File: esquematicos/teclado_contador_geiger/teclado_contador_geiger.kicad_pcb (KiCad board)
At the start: 2 copper layers, 14 parts, among them J1 Conn_01x04_Female, SW1 SW_SPST, SW2 SW_SPST, SW3 SW_SPST, SW4 SW_SPST, SW5 SW_SPST, SW6 SW_SPST

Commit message: Agregado del PCB del teclado(2)
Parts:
- J1: footprint Connector_JST:JST_EH_B04B-EH-A_1x04_P2.50mm_Vertical -> Connector_JST:JST_XH_B04B-XH-A_1x04_P2.50mm_Vertical
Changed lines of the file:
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@@
   )
   (setup
-    (last_trace_width 1.27)
+    (last_trace_width 0.25)
     (user_trace_width 1.27)
     (trace_clearance 0.2)
@@
     )
   )
-  (module Connector_JST:JST_EH_B04B-EH-A_1x04_P2.50mm_Vertical (layer B.Cu)
-    (at 130.81 102.616)
-    (descr "JST EH series connector, B04B-EH-A (http://www.jst-mfg.com/product/pdf/eng/eEH.pdf), generated with kicad-footprint-generator")
-    (tags "connector JST EH side entry")
-    (fp_text reference J1 (at 3.75 2.8) (layer B.SilkS)
-      (effects (font (size 1 1) (thickness 0.15)) (justify mirror))
-    )
-    (fp_text value Conn_01x04_Female (at 3.75 -3.4) (layer B.Fab)
-      (effects (font (size 1 1) (thickness 0.15)) (justify mirror))
-    )
-    (fp_line (start -2.5 1.6) (end -2.5 -2.2) (layer B.Fab) (width 0.1))
-    (fp_line (start -2.5 -2.2) (end 10 -2.2) (layer B.Fab) (width 0.1))
-    (fp_line (start 10 -2.2) (end 10 1.6) (layer B.Fab) (width 0.1))
-    (fp_line (start 10 1.6) (end -2.5 1.6) (layer B.Fab) (width 0.1))
-    (fp_line (start -3 2.1) (end -3 -2.7) (layer B.CrtYd) (width 0.05))
-    (fp_line (start -3 -2.7) (end 10.5 -2.7) (layer B.CrtYd) (width 0.05))
-    (fp_line (start 10.5 -2.7) (end 10.5 2.1) (layer B.CrtYd) (width 0.05))
-    (fp_line (start 10.5 2.1) (end -3 2.1) (layer B.CrtYd) (width 0.05))
-    (fp_line (start -2.61 1.71) (end -2.61 -2.31) (layer B.SilkS) (width 0.12))
-    (fp_line (start -2.61 -2.31) (end 10.11 -2.31) (layer B.SilkS) (width 0.12))
-    (fp_line (start 10.11 -2.31) (end 10.11 1.71) (layer B.SilkS) (width 0.12))
-    (fp_line (start 10.11 1.71) (end -2.61 1.71) (layer B.SilkS) (width 0.12))
-    (fp_line (start -2.61 0) (end -2.11 0) (layer B.SilkS) (width 0.12))
-    (fp_line (start -2.11 0) (end -2.11 1.21) (layer B.SilkS) (width 0.12))
-    (fp_line (start -2.11 1.21) (end 9.61 1.21) (layer B.SilkS) (width 0.12))
-    (fp_line (start 9.61 1.21) (end 9.61 0) (layer B.SilkS) (width 0.12))
-    (fp_line (start 9.61 0) (end 10.11 0) (layer B.SilkS) (width 0.12))
-    (fp_line (start -2.61 -0.81) (end -1.61 -0.81) (layer B.SilkS) (width 0.12))
-    (fp_line (start -1.61 -0.81) (end -1.61 -2.31) (layer B.SilkS) (width 0.12))
-    (fp_line (start 10.11 -0.81) (end 9.11 -0.81) (layer B.SilkS) (width 0.12))
-    (fp_line (start 9.11 -0.81) (end 9.11 -2.31) (layer B.SilkS) (width 0.12))
-    (fp_line (start -2.91 -0.11) (end -2.91 -2.61) (layer B.SilkS) (width 0.12))
-    (fp_line (start -2.91 -2.61) (end -0.41 -2.61) (layer B.SilkS) (width 0.12))
-    (fp_line (start -2.91 -0.11) (end -2.91 -2.61) (layer B.Fab) (width 0.1))
-    (fp_line (start -2.91 -2.61) (end -0.41 -2.61) (layer B.Fab) (width 0.1))
-    (fp_text user %R (at 3.75 -1.5) (layer B.Fab)
-      (effects (font (size 1 1) (thickness 0.15)) (justify mirror))
-    )
-    (pad 1 thru_hole roundrect (at 0 0) (size 1.7 1.95) (drill 0.95) (layers *.Cu *.Mask) (roundrect_rratio 0.147059)
-      (net 3 +5V))
-    (pad 2 thru_hole oval (at 2.5 0) (size 1.7 1.95) (drill 0.95) (layers *.Cu *.Mask)
-      (net 4 GND))
-    (pad 3 thru_hole oval (at 5 0) (size 1.7 1.95) (drill 0.95) (layers *.Cu *.Mask)
-      (net 5 /teclado_out))
-    (pad 4 thru_hole oval (at 7.5 0) (size 1.7 1.95) (drill 0.95) (layers *.Cu *.Mask)
-      (net 1 "Net-(D1-Pad1)"))
-    (model ${KISYS3DMOD}/Connector_JST.3dshapes/JST_EH_B04B-EH-A_1x04_P2.50mm_Vertical.wrl
-      (at (xyz 0 0 0))
-      (scale (xyz 1 1 1))
-      (rotate (xyz 0 0 0))
-    )
-  )
   (module Resistor_SMD:R_0805_2012Metric_Pad1.15x1.40mm_HandSolder (layer B.Cu)
     (at 147.066 85.852 180)
@@
       (at (xyz 0 0 0))
       (scale (xyz 1 1 1))
+      (rotate (xyz 0 0 0))
+    )
+  )
+  (module Connector_JST:JST_XH_B04B-XH-A_1x04_P2.50mm_Vertical (layer B.Cu)
+    (at 130.81 102.616)
+    (descr "JST XH series connector, B04B-XH-A (http://www.jst-mfg.com/product/pdf/eng/eXH.pdf), generated with kicad-footprint-generator")
+    (tags "connector JST XH side entry")
+    (fp_text reference J1 (at 3.75 3.55) (layer B.SilkS)
+      (effects (font (size 1 1) (thickness 0.15)) (justify mirror))
+    )
+    (fp_text value Conn_01x04_Female (at 3.75 -4.6) (layer B.Fab)
+      (effects (font (size 1 1) (thickness 0.15)) (justify mirror))
+    )
+    (fp_line (start -2.45 2.35) (end -2.45 -3.4) (layer B.Fab) (width 0.1))
+    (fp_line (start -2.45 -3.4) (end 9.95 -3.4) (layer B.Fab) (width 0.1))
+    (fp_line (start 9.95 -3.4) (end 9.95 2.35) (layer B.Fab) (width 0.1))
+    (fp_line (start 9.95 2.35) (end -2.45 2.35) (layer B.Fab) (width 0.1))
+    (fp_line (start -2.56 2.46) (end -2.56 -3.51) (layer B.SilkS) (width 0.12))
+    (fp_line (start -2.56 -3.51) (end 10.06 -3.51) (layer B.SilkS) (width 0.12))
+    (fp_line (start 10.06 -3.51) (end 10.06 2.46) (layer B.SilkS) (width 0.12))
+    (fp_line (start 10.06 2.46) (end -2.56 2.46) (layer B.SilkS) (width 0.12))
+    (fp_line (start -2.95 2.85) (end -2.95 -3.9) (layer B.CrtYd) (width 0.05))
+    (fp_line (start -2.95 -3.9) (end 10.45 -3.9) (layer B.CrtYd) (width 0.05))
+    (fp_line (start 10.45 -3.9) (end 10.45 2.85) (layer B.CrtYd) (width 0.05))
+    (fp_line (start 10.45 2.85) (end -2.95 2.85) (layer B.CrtYd) (width 0.05))
+    (fp_line (start -0.625 2.35) (end 0 1.35) (layer B.Fab) (width 0.1))
+    (fp_line (start 0 1.35) (end 0.625 2.35) (layer B.Fab) (width 0.1))
+    (fp_line (start 0.75 2.45) (end 0.75 1.7) (layer B.SilkS) (width 0.12))
+    (fp_line (start 0.75 1.7) (end 6.75 1.7) (layer B.SilkS) (width 0.12))
+    (fp_line (start 6.75 1.7) (end 6.75 2.45) (layer B.SilkS) (width 0.12))
+    (fp_line (start 6.75 2.45) (end 0.75 2.45) (layer B.SilkS) (width 0.12))
+    (fp_line (start -2.55 2.45) (end -2.55 1.7) (layer B.SilkS) (width 0.12))
+    (fp_line (start -2.55 1.7) (end -0.75 1.7) (layer B.SilkS) (width 0.12))
+    (fp_line (start -0.75 1.7) (end -0.75 2.45) (layer B.SilkS) (width 0.12))
+    (fp_line (start -0.75 2.45) (end -2.55 2.45) (layer B.SilkS) (width 0.12))
+    (fp_line (start 8.25 2.45) (end 8.25 1.7) (layer B.SilkS) (width 0.12))
+    (fp_line (start 8.25 1.7) (end 10.05 1.7) (layer B.SilkS) (width 0.12))
+    (fp_line (start 10.05 1.7) (end 10.05 2.45) (layer B.SilkS) (width 0.12))
+    (fp_line (start 10.05 2.45) (end 8.25 2.45) (layer B.SilkS) (width 0.12))
+    (fp_line (start -2.55 0.2) (end -1.8 0.2) (layer B.SilkS) (width 0.12))
+    (fp_line (start -1.8 0.2) (end -1.8 -2.75) (layer B.SilkS) (width 0.12))
+    (fp_line (start -1.8 -2.75) (end 3.75 -2.75) (layer B.SilkS) (width 0.12))
+    (fp_line (start 10.05 0.2) (end 9.3 0.2) (layer B.SilkS) (width 0.12))
+    (fp_line (start 9.3 0.2) (end 9.3 -2.75) (layer B.SilkS) (width 0.12))
+    (fp_line (start 9.3 -2.75) (end 3.75 -2.75) (layer B.SilkS) (width 0.12))
+    (fp_line (start -1.6 2.75) (end -2.85 2.75) (layer B.SilkS) (width 0.12))
+    (fp_line (start -2.85 2.75) (end -2.85 1.5) (layer B.SilkS) (width 0.12))
+    (fp_text user %R (at 3.75 -2.7) (layer B.Fab)
+      (effects (font (size 1 1) (thickness 0.15)) (justify mirror))
+    )
+    (pad 1 thru_hole roundrect (at 0 0) (size 1.7 1.95) (drill 0.95) (layers *.Cu *.Mask) (roundrect_rratio 0.147059)
+      (net 3 +5V))
+    (pad 2 thru_hole oval (at 2.5 0) (size 1.7 1.95) (drill 0.95) (layers *.Cu *.Mask)
+      (net 4 GND))
+    (pad 3 thru_hole oval (at 5 0) (size 1.7 1.95) (drill 0.95) (layers *.Cu *.Mask)
+      (net 5 /teclado_out))
+    (pad 4 thru_hole oval (at 7.5 0) (size 1.7 1.95) (drill 0.95) (layers *.Cu *.Mask)
+      (net 1 "Net-(D1-Pad1)"))
+    (model ${KISYS3DMOD}/Connector_JST.3dshapes/JST_XH_B04B-XH-A_1x04_P2.50mm_Vertical.wrl
+      (at (xyz 0 0 0))
+      (scale (xyz 1 1 1))

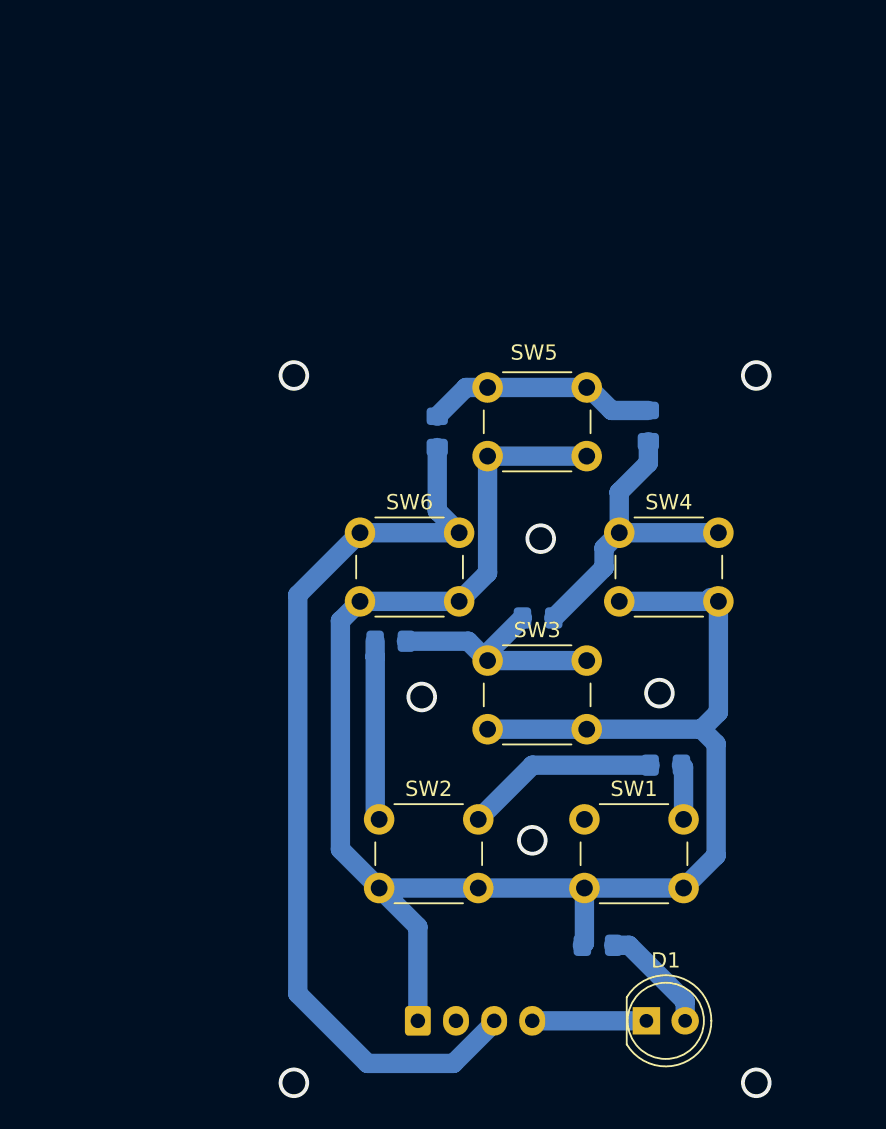
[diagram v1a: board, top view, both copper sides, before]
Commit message: Agregado de LED verde a la placa del teclado e incremento de las dimensiones de esta última incluyendo una mayor separación entre los botones
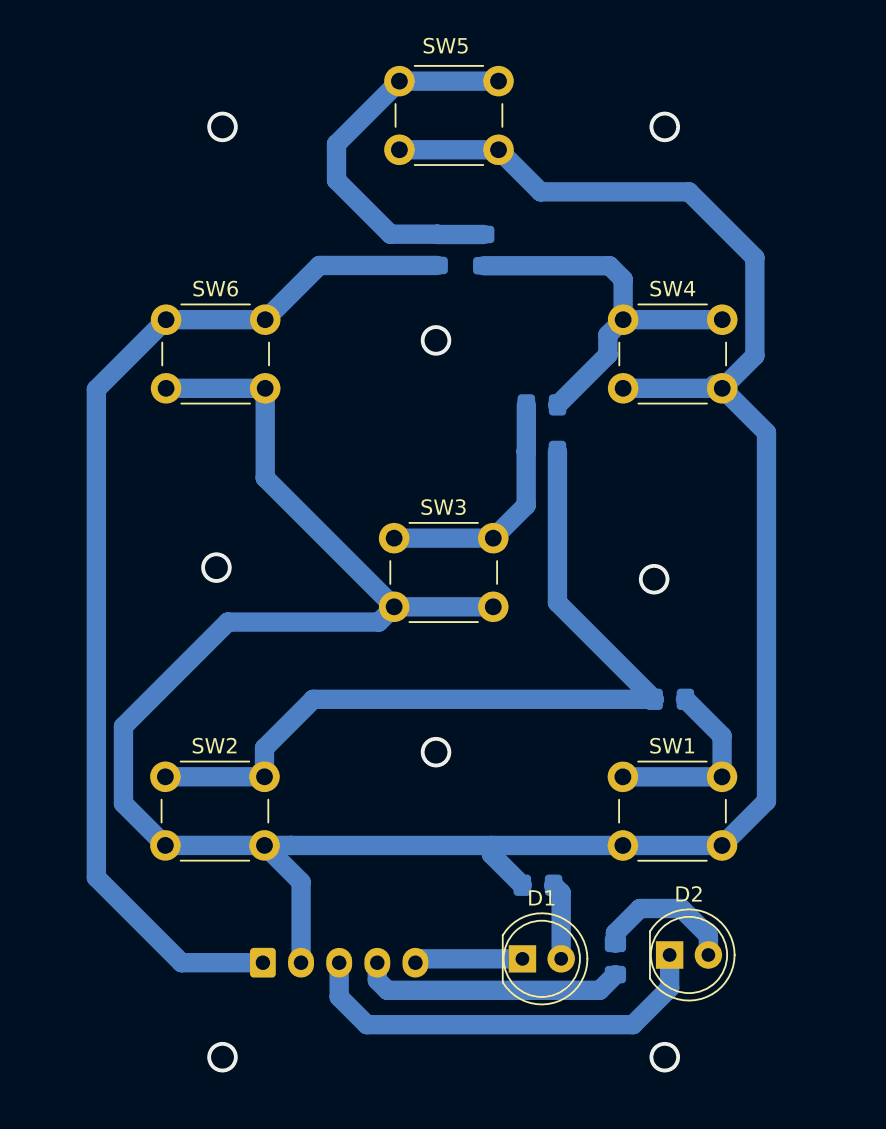
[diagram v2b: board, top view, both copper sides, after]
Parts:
- added D2: LED VERDE, LED_THT:LED_D5.0mm, F.Cu at (147.3, 98.3)
- added R7: 220, Resistor_SMD:R_0805_2012Metric_Pad1.15x1.40mm_HandSolder, B.Cu at (143.8, 98.6)
- D1: value LED -> LED ROJO
- J1: value Conn_01x04_Female -> Conn_01x05_Female; footprint Connector_JST:JST_XH_B04B-XH-A_1x04_P2.50mm_Vertical -> Connector_JST:JST_XH_B05B-XH-A_1x05_P2.50mm_Vertical
- moved SW5 20.9 mm to (129.6, 41.0)
- moved SW6 18.9 mm to (114.3, 56.6)
- moved R2 15.9 mm to (138.9, 65.3), turned to 180 degrees
- moved R4 15.8 mm to (135.1, 52.1)
- moved SW2 14.3 mm to (114.3, 86.6)
- moved R3 14.0 mm to (138.9, 62.2)
- moved SW4 14.0 mm to (144.3, 56.6)
- moved R5 11.9 mm to (132.1, 52.1)
- moved J1 10.9 mm to (120.7, 98.8)
- moved SW3 10.1 mm to (129.3, 71.0)
- moved D1 9.09 mm to (137.7, 98.6)
- moved R6 5.57 mm to (138.7, 93.7)
- moved R1 4.33 mm to (147.3, 81.5)
- moved SW1 3.76 mm to (144.3, 86.6)
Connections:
- J1 pad 1: +5V -> /teclado_out
- J1 pad 2: GND -> +5V
- J1 pad 3: /teclado_out -> GND
- J1 pad 4: Net-(D1-Pad1) -> Net-(J1-Pad4)
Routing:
- net +5V: track 118.6 -> 184.5 mm
- net Net-(R1-Pad2): track 24.5 -> 54.1 mm
- net GND: track 0.00 -> 27.8 mm
- net Net-(J1-Pad4): track 0.00 -> 17.5 mm
- net Net-(R4-Pad2): track 15.1 -> 25.8 mm
- net /teclado_out: track 60.6 -> 71.1 mm
- net Net-(D2-Pad2): track 0.00 -> 9.45 mm
- net Net-(R1-Pad1): track 3.61 -> 12.6 mm
- net Net-(R3-Pad2): track 20.6 -> 26.0 mm
- net Net-(D1-Pad2): track 7.49 -> 5.03 mm

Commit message: Agrega PCB del teclado
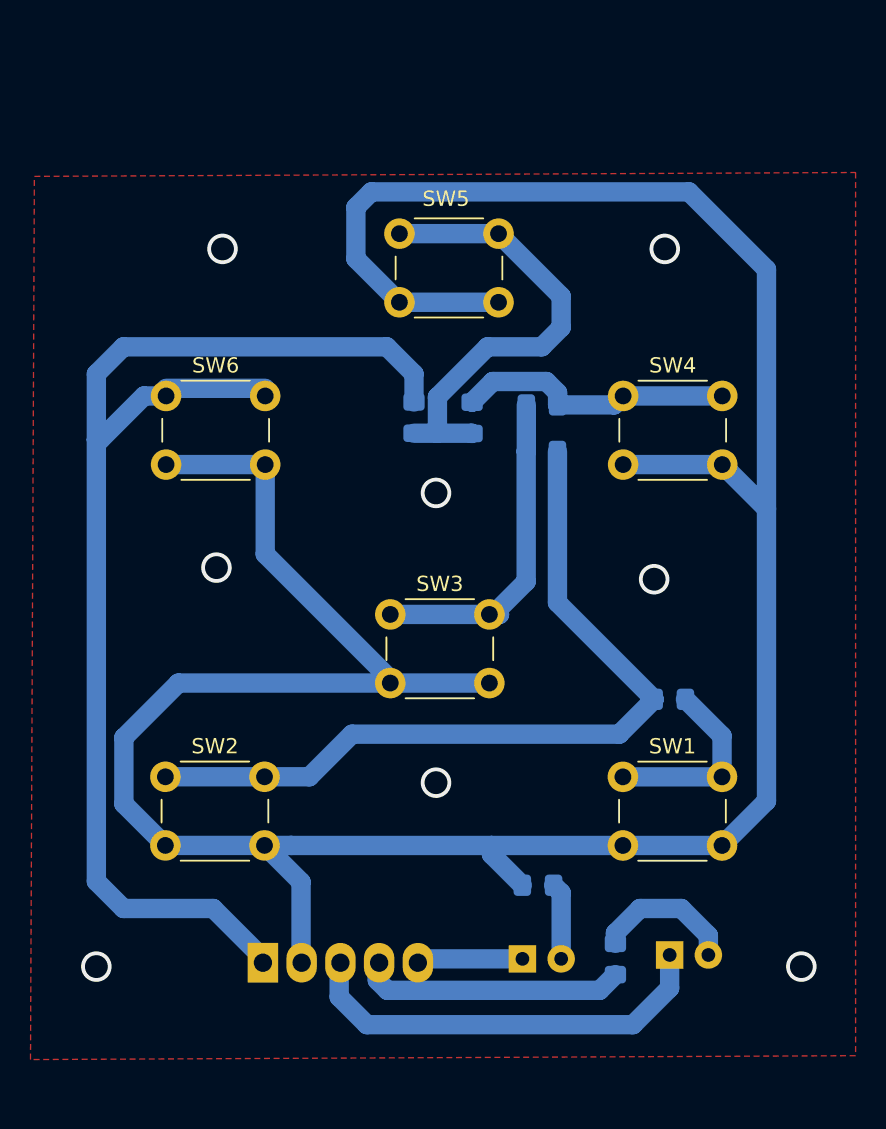
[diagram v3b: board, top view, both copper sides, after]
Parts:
- D1, D2: moved to B.Cu
- J1: footprint Connector_JST:JST_XH_B05B-XH-A_1x05_P2.50mm_Vertical -> Connectors_Molex:Molex_KK-6410-05_05x2.54mm_Straight
- moved R5 11.1 mm to (130.6, 63.1), turned to 90 degrees
- moved R4 11.0 mm to (134.4, 63.1), turned to 270 degrees
- moved SW5 10.0 mm to (129.6, 51.0)
- moved SW3 5.01 mm to (129.0, 76.0)
- moved SW4 5.00 mm to (144.3, 61.6)
- moved SW6 5.00 mm to (114.3, 61.6)
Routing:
- net +5V: track 184.5 -> 199.9 mm
- net /teclado_out: track 71.1 -> 83.1 mm
- net Net-(R3-Pad2): track 26.0 -> 18.3 mm
- net Net-(R2-Pad2): track 16.1 -> 22.0 mm
- net Net-(R4-Pad2): track 25.8 -> 30.6 mm
- net Net-(R1-Pad2): track 54.1 -> 53.0 mm
- net GND: vias 0 -> 8
- net (no net): vias 8 -> 0
- added copper zone on F.Cu, net GND

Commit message: Se modificó distancia entre dos resistencias de la placa teclado
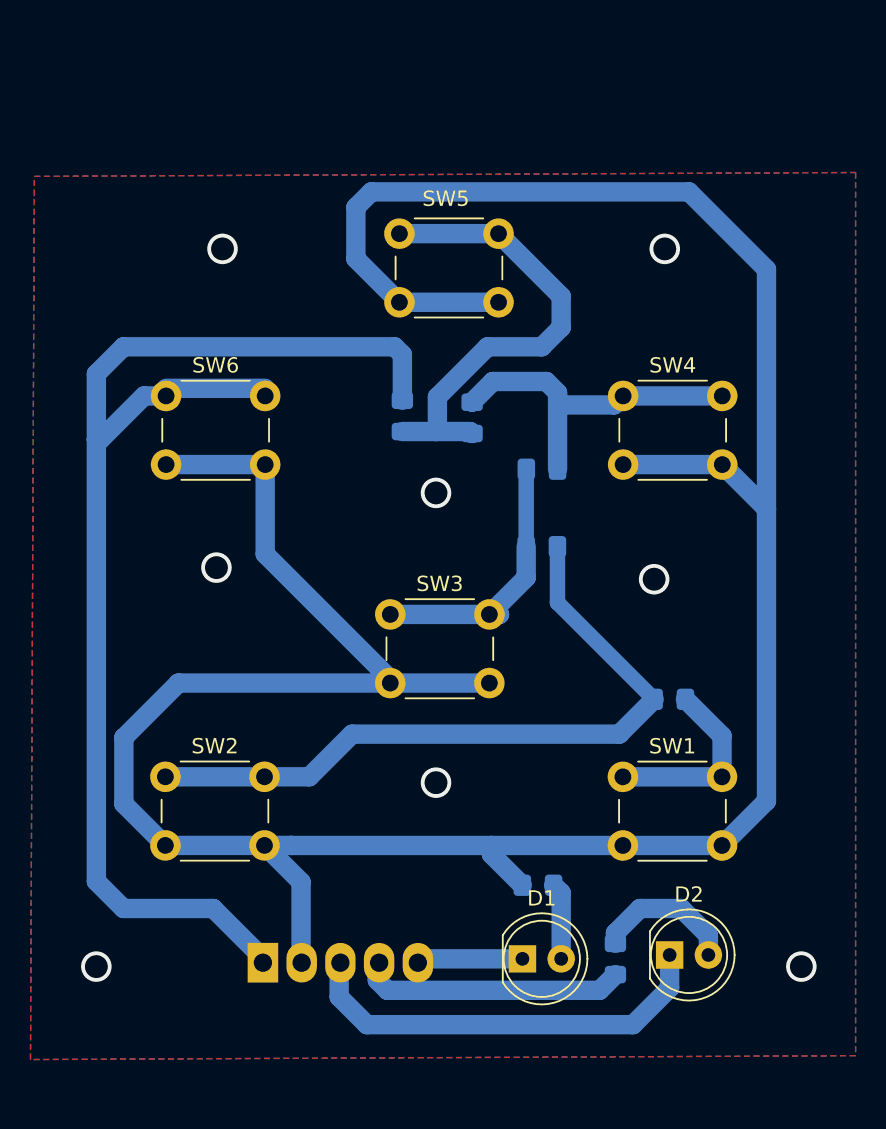
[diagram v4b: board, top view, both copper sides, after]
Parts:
- D1, D2: moved to F.Cu
- moved R2 6.25 mm to (138.9, 71.5)
- moved R3 4.22 mm to (138.9, 66.4)
- moved R5 0.77 mm to (129.8, 63.0)
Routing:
- net Net-(R1-Pad2): track 53.0 -> 46.8 mm
- net Net-(R3-Pad2): track 18.3 -> 22.6 mm
- net Net-(R2-Pad2): track 22.0 -> 17.8 mm
- net Net-(R4-Pad2): track 30.6 -> 31.3 mm
- added copper zone on B.Cu, net GND
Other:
- net class Default: clearance 0.2 -> 1
- rule trace_clearance: 0.2 -> 1
